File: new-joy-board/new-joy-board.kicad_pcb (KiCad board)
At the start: 2 copper layers, 61 x 139.2 mm, 44 parts, among them J0 SDS-50J, J1 SDS-50J, J2 SDS-50J, J3 SDS-50J, J4 BAT, U0 P82B715, U1 P82B715, U10 oskj-dc-dc, U2 P82B715, U3 P82B715, U4 AZReady_ESP32, U5 24L01, U7 MPU6050_Breakout

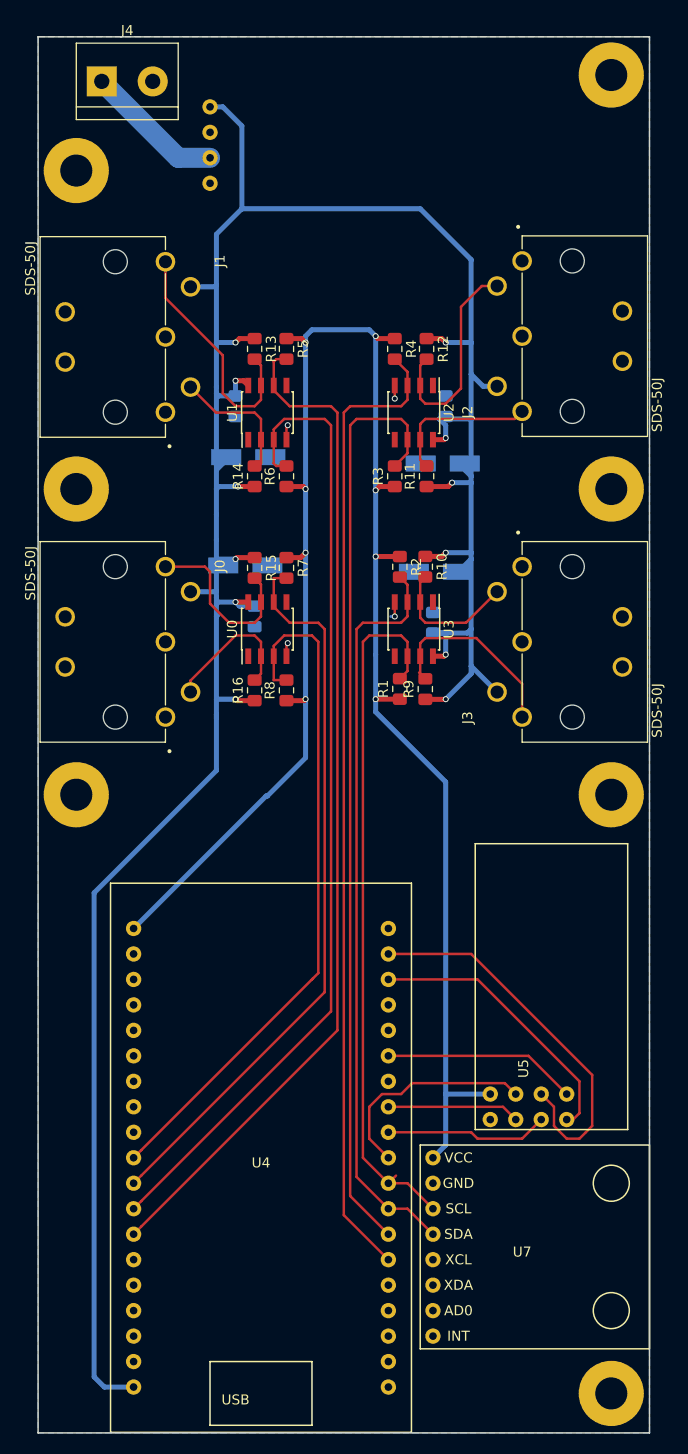
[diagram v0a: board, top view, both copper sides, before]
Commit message: Exchanged new footprints with bigger pads in the boards
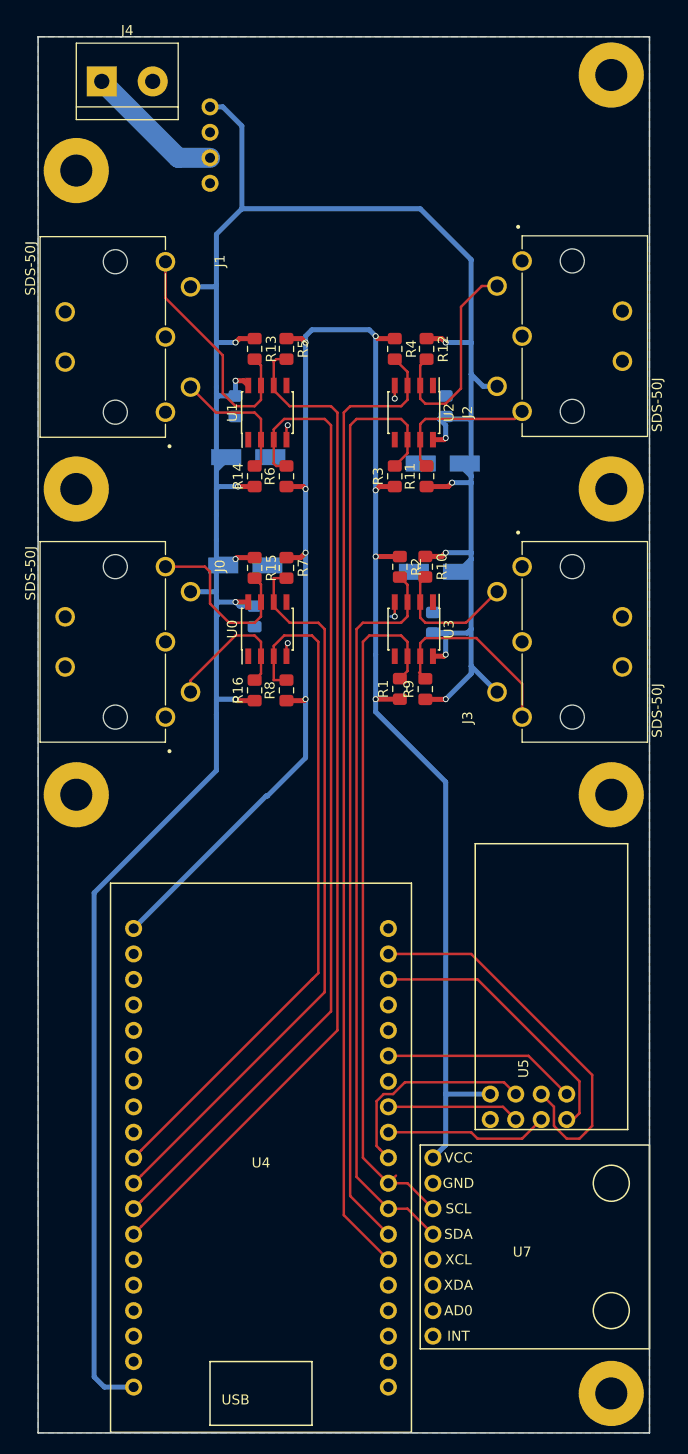
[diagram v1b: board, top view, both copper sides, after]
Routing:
- net /CS0: track 21.9 -> 21.3 mm
